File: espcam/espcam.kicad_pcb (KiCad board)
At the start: 2 copper layers, 40.6 x 25.4 mm, 3 parts, among them J1 Conn1, J2 Conn2, U1 ESPCAM

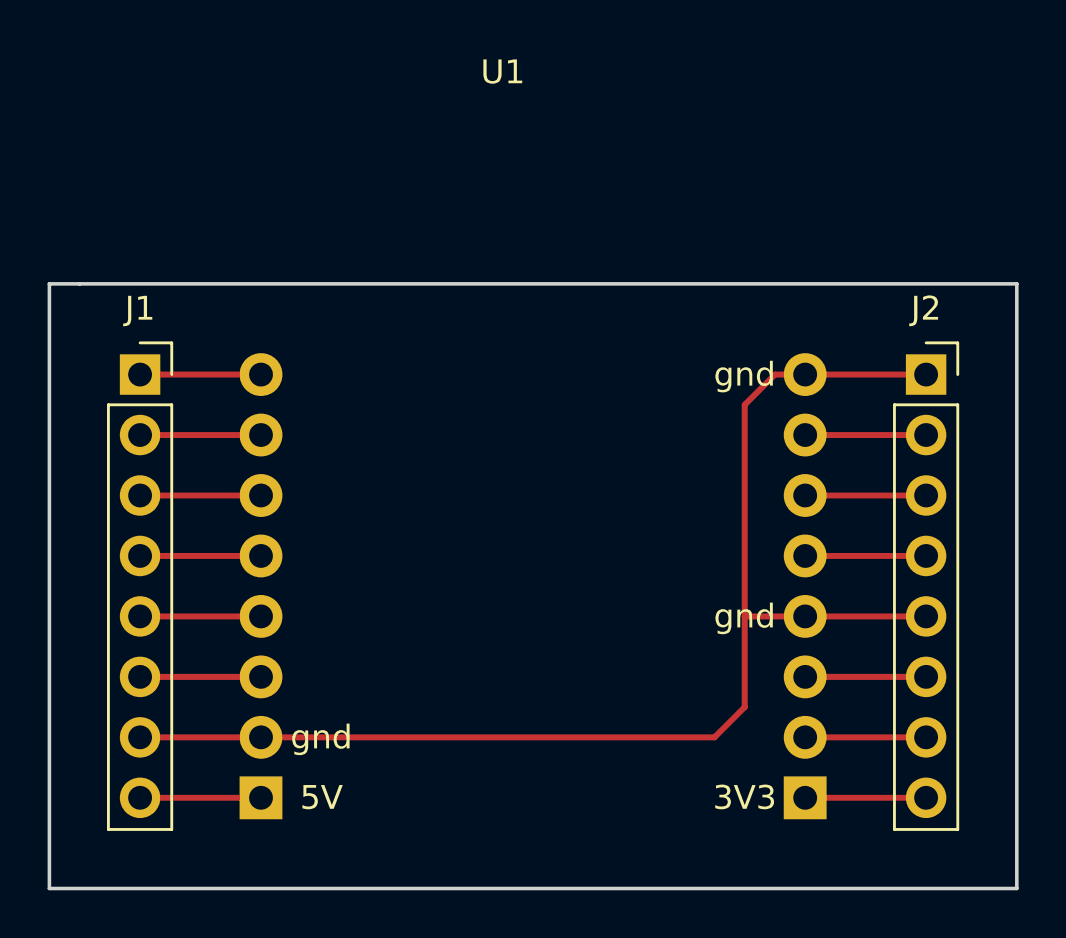
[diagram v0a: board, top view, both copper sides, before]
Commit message: Fix Footprints for kicad 5.1.8
thanks to tobi for the tip how to install a newer
kicad on debian: there is a newer version in
debian-packports.

fixed the libraries and footprints, and changed
the path to relative ones.
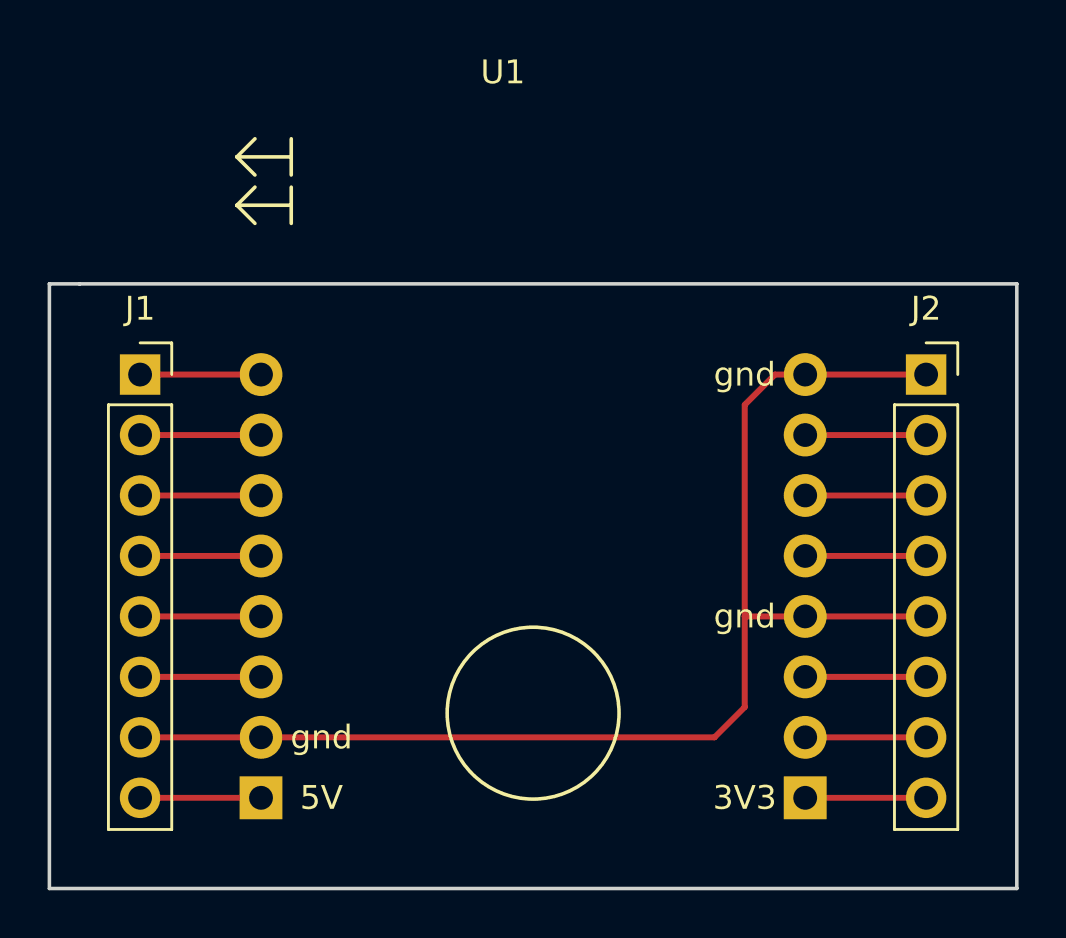
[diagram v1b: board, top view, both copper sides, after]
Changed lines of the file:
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@@
-(kicad_pcb (version 20171130) (host pcbnew 5.0.2+dfsg1-1)
+(kicad_pcb (version 20171130) (host pcbnew 5.1.8+dfsg1-1~bpo10+1)
   (general
     (thickness 1.6)
@@
     (zone_45_only no)
     (trace_min 0.2)
-    (segment_width 0.2)
-    (edge_width 0.15)
     (via_size 0.8)
     (via_drill 0.4)
@@
     (uvia_min_size 0.2)
     (uvia_min_drill 0.1)
+    (edge_width 0.15)
+    (segment_width 0.2)
     (pcb_text_width 0.3)
     (pcb_text_size 1.5 1.5)
@@
       (effects (font (size 1 1) (thickness 0.15)))
     )
+    (fp_line (start -1.8 19.55) (end -1.8 -1.8) (layer F.CrtYd) (width 0.05))
+    (fp_line (start 1.75 19.55) (end -1.8 19.55) (layer F.CrtYd) (width 0.05))
+    (fp_line (start 1.75 -1.8) (end 1.75 19.55) (layer F.CrtYd) (width 0.05))
+    (fp_line (start -1.8 -1.8) (end 1.75 -1.8) (layer F.CrtYd) (width 0.05))
+    (fp_line (start 0 -1.33) (end 1.33 -1.33) (layer F.SilkS) (width 0.12))
+    (fp_line (start 1.33 -1.33) (end 1.33 0) (layer F.SilkS) (width 0.12))
+    (fp_line (start 1.33 1.27) (end 1.33 19.11) (layer F.SilkS) (width 0.12))
+    (fp_line (start -1.33 19.11) (end 1.33 19.11) (layer F.SilkS) (width 0.12))
+    (fp_line (start -1.33 1.27) (end -1.33 19.11) (layer F.SilkS) (width 0.12))
+    (fp_line (start -1.33 1.27) (end 1.33 1.27) (layer F.SilkS) (width 0.12))
+    (fp_line (start -1.27 19.05) (end -1.27 -1.27) (layer F.Fab) (width 0.1))
+    (fp_line (start 1.27 19.05) (end -1.27 19.05) (layer F.Fab) (width 0.1))
+    (fp_line (start 1.27 -0.635) (end 1.27 19.05) (layer F.Fab) (width 0.1))
+    (fp_line (start 0.635 -1.27) (end 1.27 -0.635) (layer F.Fab) (width 0.1))
     (fp_line (start -1.27 -1.27) (end 0.635 -1.27) (layer F.Fab) (width 0.1))
-    (fp_line (start 0.635 -1.27) (end 1.27 -0.635) (layer F.Fab) (width 0.1))
-    (fp_line (start 1.27 -0.635) (end 1.27 19.05) (layer F.Fab) (width 0.1))
-    (fp_line (start 1.27 19.05) (end -1.27 19.05) (layer F.Fab) (width 0.1))
-    (fp_line (start -1.27 19.05) (end -1.27 -1.27) (layer F.Fab) (width 0.1))
-    (fp_line (start -1.33 1.27) (end 1.33 1.27) (layer F.SilkS) (width 0.12))
-    (fp_line (start -1.33 1.27) (end -1.33 19.11) (layer F.SilkS) (width 0.12))
-    (fp_line (start -1.33 19.11) (end 1.33 19.11) (layer F.SilkS) (width 0.12))
-    (fp_line (start 1.33 1.27) (end 1.33 19.11) (layer F.SilkS) (width 0.12))
-    (fp_line (start 1.33 -1.33) (end 1.33 0) (layer F.SilkS) (width 0.12))
-    (fp_line (start 0 -1.33) (end 1.33 -1.33) (layer F.SilkS) (width 0.12))
-    (fp_line (start -1.8 -1.8) (end 1.75 -1.8) (layer F.CrtYd) (width 0.05))
-    (fp_line (start 1.75 -1.8) (end 1.75 19.55) (layer F.CrtYd) (width 0.05))
-    (fp_line (start 1.75 19.55) (end -1.8 19.55) (layer F.CrtYd) (width 0.05))
-    (fp_line (start -1.8 19.55) (end -1.8 -1.8) (layer F.CrtYd) (width 0.05))
     (fp_text user %R (at 0 8.89 90) (layer F.Fab)
       (effects (font (size 1 1) (thickness 0.15)))
@@
       (effects (font (size 1 1) (thickness 0.15)))
     )
+    (fp_line (start -1.27 -1.27) (end 0.635 -1.27) (layer F.Fab) (width 0.1))
+    (fp_line (start 0.635 -1.27) (end 1.27 -0.635) (layer F.Fab) (width 0.1))
+    (fp_line (start 1.27 -0.635) (end 1.27 19.05) (layer F.Fab) (width 0.1))
+    (fp_line (start 1.27 19.05) (end -1.27 19.05) (layer F.Fab) (width 0.1))
+    (fp_line (start -1.27 19.05) (end -1.27 -1.27) (layer F.Fab) (width 0.1))
+    (fp_line (start -1.33 1.27) (end 1.33 1.27) (layer F.SilkS) (width 0.12))
+    (fp_line (start -1.33 1.27) (end -1.33 19.11) (layer F.SilkS) (width 0.12))
+    (fp_line (start -1.33 19.11) (end 1.33 19.11) (layer F.SilkS) (width 0.12))
+    (fp_line (start 1.33 1.27) (end 1.33 19.11) (layer F.SilkS) (width 0.12))
+    (fp_line (start 1.33 -1.33) (end 1.33 0) (layer F.SilkS) (width 0.12))
+    (fp_line (start 0 -1.33) (end 1.33 -1.33) (layer F.SilkS) (width 0.12))
+    (fp_line (start -1.8 -1.8) (end 1.75 -1.8) (layer F.CrtYd) (width 0.05))
+    (fp_line (start 1.75 -1.8) (end 1.75 19.55) (layer F.CrtYd) (width 0.05))
+    (fp_line (start 1.75 19.55) (end -1.8 19.55) (layer F.CrtYd) (width 0.05))
+    (fp_line (start -1.8 19.55) (end -1.8 -1.8) (layer F.CrtYd) (width 0.05))
     (fp_text user %R (at 0 8.89 90) (layer F.Fab)
       (effects (font (size 1 1) (thickness 0.15)))
     )
-    (fp_line (start -1.8 19.55) (end -1.8 -1.8) (layer F.CrtYd) (width 0.05))
-    (fp_line (start 1.75 19.55) (end -1.8 19.55) (layer F.CrtYd) (width 0.05))
-    (fp_line (start 1.75 -1.8) (end 1.75 19.55) (layer F.CrtYd) (width 0.05))
-    (fp_line (start -1.8 -1.8) (end 1.75 -1.8) (layer F.CrtYd) (width 0.05))
-    (fp_line (start 0 -1.33) (end 1.33 -1.33) (layer F.SilkS) (width 0.12))
-    (fp_line (start 1.33 -1.33) (end 1.33 0) (layer F.SilkS) (width 0.12))
-    (fp_line (start 1.33 1.27) (end 1.33 19.11) (layer F.SilkS) (width 0.12))
-    (fp_line (start -1.33 19.11) (end 1.33 19.11) (layer F.SilkS) (width 0.12))
-    (fp_line (start -1.33 1.27) (end -1.33 19.11) (layer F.SilkS) (width 0.12))
-    (fp_line (start -1.33 1.27) (end 1.33 1.27) (layer F.SilkS) (width 0.12))
-    (fp_line (start -1.27 19.05) (end -1.27 -1.27) (layer F.Fab) (width 0.1))
-    (fp_line (start 1.27 19.05) (end -1.27 19.05) (layer F.Fab) (width 0.1))
-    (fp_line (start 1.27 -0.635) (end 1.27 19.05) (layer F.Fab) (width 0.1))
-    (fp_line (start 0.635 -1.27) (end 1.27 -0.635) (layer F.Fab) (width 0.1))
-    (fp_line (start -1.27 -1.27) (end 0.635 -1.27) (layer F.Fab) (width 0.1))
     (pad 8 thru_hole oval (at 0 17.78) (size 1.7 1.7) (drill 1) (layers *.Cu *.Mask)
       (net 14 3.3V))
@@
       (effects (font (size 1 1) (thickness 0.15)))
     )
-    (fp_text value ESPCAM (at 11.43 0) (layer F.Fab)
-      (effects (font (size 1 1) (thickness 0.15)))
-    )
-    (fp_text user gnd (at 10.16 2.54) (layer F.SilkS)
-      (effects (font (size 1 1) (thickness 0.15)))
-    )
+    (fp_text value ESPCAM (at 0 -12.7) (layer F.Fab)
+      (effects (font (size 1 1) (thickness 0.15)))
+    )
+    (fp_line (start -8.89 -5.334) (end -8.89 -3.81) (layer F.SilkS) (width 0.15))
+    (fp_line (start -8.89 -7.366) (end -8.89 -5.842) (layer F.SilkS) (width 0.15))
+    (fp_line (start -11.176 -6.604) (end -8.89 -6.604) (layer F.SilkS) (width 0.15))
+    (fp_line (start -11.176 -6.604) (end -10.414 -7.366) (layer F.SilkS) (width 0.15))
+    (fp_line (start -10.414 -5.842) (end -11.176 -6.604) (layer F.SilkS) (width 0.15))
+    (fp_line (start -11.176 -4.572) (end -10.414 -3.81) (layer F.SilkS) (width 0.15))
+    (fp_line (start -11.176 -4.572) (end -10.414 -5.334) (layer F.SilkS) (width 0.15))
+    (fp_line (start -8.89 -4.572) (end -11.176 -4.572) (layer F.SilkS) (width 0.15))
+    (fp_circle (center 1.27 16.764) (end 3.556 19.558) (layer F.SilkS) (width 0.15))
     (fp_line (start -12.7 22.86) (end -12.7 -12.7) (layer B.Paste) (width 0.15))
     (fp_line (start -10.16 -15.24) (end 12.7 -15.24) (layer B.Paste) (width 0.15))
     (fp_line (start 15.24 -12.7) (end 15.24 22.86) (layer B.Paste) (width 0.15))
     (fp_line (start 12.7 25.4) (end -10.16 25.4) (layer B.Paste) (width 0.15))
-    (fp_arc (start -10.16 22.86) (end -12.7 22.86) (angle -90) (layer B.Paste) (width 0.15))
-    (fp_arc (start 12.7 22.86) (end 12.7 25.4) (angle -90) (layer B.Paste) (width 0.15))
-    (fp_arc (start 12.7 -12.7) (end 15.24 -12.7) (angle -90) (layer B.Paste) (width 0.15))
-    (fp_arc (start -10.16 -12.7) (end -10.16 -15.24) (angle -90) (layer B.Paste) (width 0.15))
-    (fp_text user gnd (at 10.16 12.7) (layer F.SilkS)
-      (effects (font (size 1 1) (thickness 0.15)))
-    )
-    (fp_text user 3V3 (at 10.16 20.32) (layer F.SilkS)
-      (effects (font (size 1 1) (thickness 0.15)))
-    )
-    (fp_text user gnd (at -7.62 17.78) (layer F.SilkS)
-      (effects (font (size 1 1) (thickness 0.15)))
-    )
-    (fp_text user 5V (at -7.62 20.32) (layer F.SilkS)
-      (effects (font (size 1 1) (thickness 0.15)))
-    )
     (fp_line (start -11.43 1.27) (end -8.89 1.27) (layer F.CrtYd) (width 0.15))
     (fp_line (start -8.89 1.27) (end -8.89 21.59) (layer F.CrtYd) (width 0.15))
@@
     (fp_line (start -8.89 21.59) (end -11.43 21.59) (layer B.CrtYd) (width 0.15))
     (fp_line (start -11.43 21.59) (end -11.43 1.27) (layer B.CrtYd) (width 0.15))
+    (fp_text user gnd (at 10.16 2.54) (layer F.SilkS)
+      (effects (font (size 1 1) (thickness 0.15)))
+    )
+    (fp_arc (start -10.16 22.86) (end -12.7 22.86) (angle -90) (layer B.Paste) (width 0.15))
+    (fp_arc (start 12.7 22.86) (end 12.7 25.4) (angle -90) (layer B.Paste) (width 0.15))
+    (fp_arc (start 12.7 -12.7) (end 15.24 -12.7) (angle -90) (layer B.Paste) (width 0.15))
+    (fp_arc (start -10.16 -12.7) (end -10.16 -15.24) (angle -90) (layer B.Paste) (width 0.15))
+    (fp_text user gnd (at 10.16 12.7) (layer F.SilkS)
+      (effects (font (size 1 1) (thickness 0.15)))
+    )
+    (fp_text user 3V3 (at 10.16 20.32) (layer F.SilkS)
+      (effects (font (size 1 1) (thickness 0.15)))
+    )
+    (fp_text user gnd (at -7.62 17.78) (layer F.SilkS)
+      (effects (font (size 1 1) (thickness 0.15)))
+    )
+    (fp_text user 5V (at -7.62 20.32) (layer F.SilkS)
+      (effects (font (size 1 1) (thickness 0.15)))
+    )
     (pad 1 thru_hole circle (at -10.16 2.54) (size 1.8 1.8) (drill 1) (layers *.Cu *.Mask)
       (net 1 "Net-(J1-Pad1)"))
